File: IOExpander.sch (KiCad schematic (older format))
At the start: 2 parts

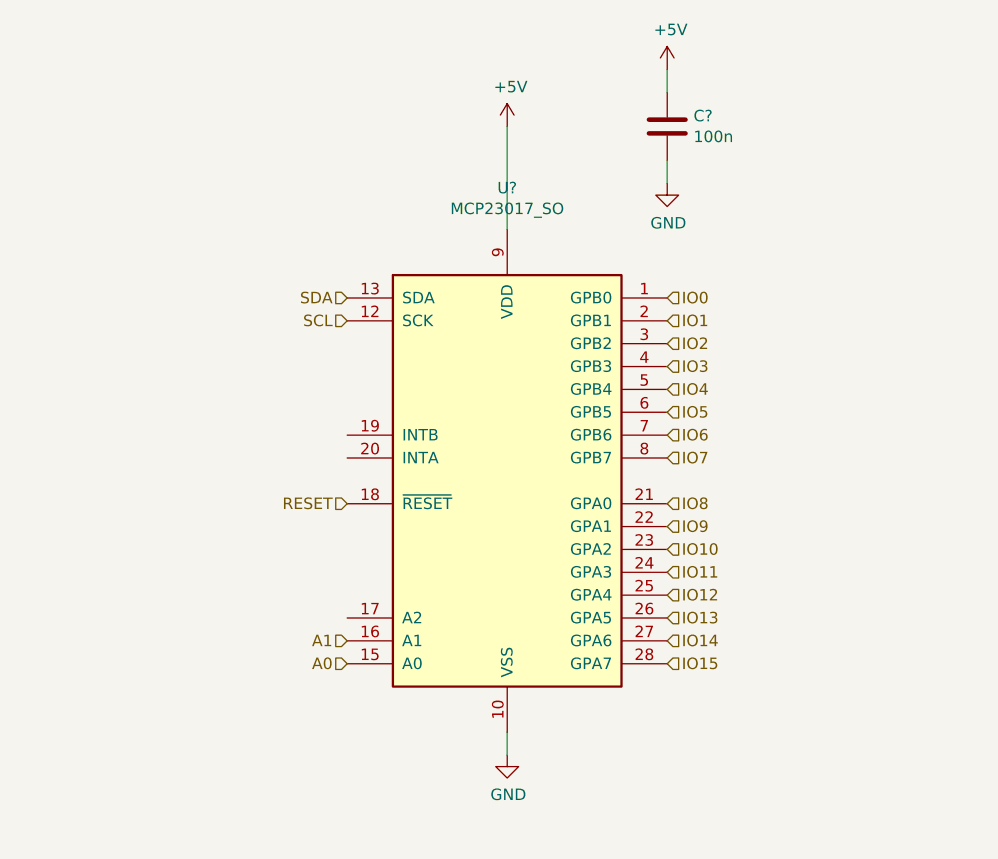
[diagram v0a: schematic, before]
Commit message: added display pinout
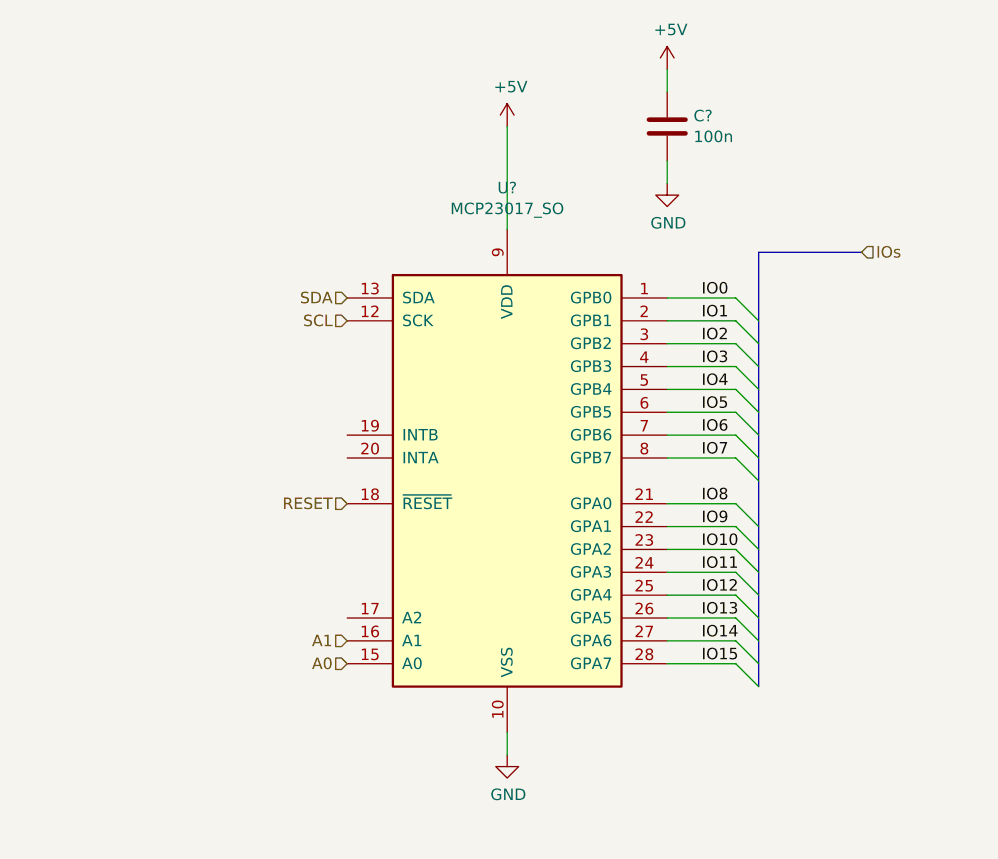
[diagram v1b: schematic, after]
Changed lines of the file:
@@
 $Descr A4 11693 8268
 encoding utf-8
-Sheet 4 4
+Sheet 4 6
 Title ""
 Date ""
@@
 Comment4 ""
 $EndDescr
-$Comp
-L Interface_Expansion:MCP23017_SO U?
-U 1 1 607270E1
-P 4450 3100
-F 0 "U?" H 4450 4381 50  0000 C CNN
-F 1 "MCP23017_SO" H 4450 4290 50  0000 C CNN
-F 2 "Package_SO:SOIC-28W_7.5x17.9mm_P1.27mm" H 4650 2100 50  0001 L CNN
-F 3 "http://ww1.microchip.com/downloads/en/DeviceDoc/20001952C.pdf" H 4650 2000 50  0001 L CNN
-	1    4450 3100
-	1    0    0    -1
-$EndComp
 Text HLabel 3750 2300 0    50   Input ~ 0
 SDA
@@
 U 1 1 607285C4
 P 4450 4300
+AR Path="/607267A8/607285C4" Ref="#PWR?"  Part="1"
+AR Path="/60679D69/607285C4" Ref="#PWR?"  Part="1"
 F 0 "#PWR?" H 4450 4050 50  0001 C CNN
 F 1 "GND" H 4455 4127 50  0000 C CNN
@@
 U 1 1 60728B72
 P 4450 1550
+AR Path="/607267A8/60728B72" Ref="#PWR?"  Part="1"
+AR Path="/60679D69/60728B72" Ref="#PWR?"  Part="1"
 F 0 "#PWR?" H 4450 1400 50  0001 C CNN
 F 1 "+5V" H 4465 1723 50  0000 C CNN
@@
 U 1 1 60729756
 P 5150 1550
+AR Path="/607267A8/60729756" Ref="C?"  Part="1"
+AR Path="/60679D69/60729756" Ref="C?"  Part="1"
 F 0 "C?" H 5265 1596 50  0000 L CNN
 F 1 "100n" H 5265 1505 50  0000 L CNN
@@
 U 1 1 60729F21
 P 5150 1300
+AR Path="/607267A8/60729F21" Ref="#PWR?"  Part="1"
+AR Path="/60679D69/60729F21" Ref="#PWR?"  Part="1"
 F 0 "#PWR?" H 5150 1150 50  0001 C CNN
 F 1 "+5V" H 5165 1473 50  0000 C CNN
@@
 U 1 1 6072A25B
 P 5150 1800
+AR Path="/607267A8/6072A25B" Ref="#PWR?"  Part="1"
+AR Path="/60679D69/6072A25B" Ref="#PWR?"  Part="1"
 F 0 "#PWR?" H 5150 1550 50  0001 C CNN
 F 1 "GND" H 5155 1627 50  0000 C CNN
@@
 Wire Wire Line
 	5150 1700 5150 1800
-Text HLabel 5150 2300 2    50   Input ~ 0
+$Comp
+L Interface_Expansion:MCP23017_SO U?
+U 1 1 607270E1
+P 4450 3100
+AR Path="/607267A8/607270E1" Ref="U?"  Part="1"
+AR Path="/60679D69/607270E1" Ref="U?"  Part="1"
+F 0 "U?" H 4450 4381 50  0000 C CNN
+F 1 "MCP23017_SO" H 4450 4290 50  0000 C CNN
+F 2 "Package_SO:SOIC-28W_7.5x17.9mm_P1.27mm" H 4650 2100 50  0001 L CNN
+F 3 "http://ww1.microchip.com/downloads/en/DeviceDoc/20001952C.pdf" H 4650 2000 50  0001 L CNN
+	1    4450 3100
+	1    0    0    -1
+$EndComp
+Wire Wire Line
+	5450 2300 5150 2300
+Wire Wire Line
+	5450 2400 5150 2400
+Wire Wire Line
+	5450 2500 5150 2500
+Wire Wire Line
+	5450 2600 5150 2600
+Wire Wire Line
+	5450 2700 5150 2700
+Wire Wire Line
+	5450 2800 5150 2800
+Wire Wire Line
+	5450 2900 5150 2900
+Wire Wire Line
+	5450 3000 5150 3000
+Wire Wire Line
+	5450 3200 5150 3200
+Wire Wire Line
+	5450 3300 5150 3300
+Wire Wire Line
+	5450 3400 5150 3400
+Wire Wire Line
+	5450 3500 5150 3500
+Wire Wire Line
+	5450 3600 5150 3600
+Wire Wire Line
+	5450 3700 5150 3700
+Wire Wire Line
+	5450 3800 5150 3800
+Wire Wire Line
+	5450 3900 5150 3900
+Wire Bus Line
+	5550 2100 6000 2100
+Entry Wire Line
+	5450 2300 5550 2400
+Entry Wire Line
+	5450 2400 5550 2500
+Entry Wire Line
+	5450 2500 5550 2600
+Entry Wire Line
+	5450 2600 5550 2700
+Entry Wire Line
+	5450 2700 5550 2800
+Entry Wire Line
+	5450 2800 5550 2900
+Entry Wire Line
+	5450 2900 5550 3000
+Entry Wire Line
+	5450 3000 5550 3100
+Entry Wire Line
+	5450 3200 5550 3300
+Entry Wire Line
+	5450 3300 5550 3400
+Entry Wire Line
+	5450 3400 5550 3500
+Entry Wire Line
+	5450 3500 5550 3600
+Entry Wire Line
+	5450 3600 5550 3700
+Entry Wire Line
+	5450 3700 5550 3800
+Entry Wire Line
+	5450 3800 5550 3900
+Entry Wire Line
+	5450 3900 5550 4000
+Wire Bus Line
+	5550 2100 5550 4000
+Text HLabel 6000 2100 2    50   Input ~ 0
+IOs
+Text Label 5300 2300 0    50   ~ 0
 IO0
-Text HLabel 5150 2400 2    50   Input ~ 0
+Text Label 5300 2400 0    50   ~ 0
 IO1
-Text HLabel 5150 2500 2    50   Input ~ 0
+Text Label 5300 2500 0    50   ~ 0
 IO2
-Text HLabel 5150 2600 2    50   Input ~ 0
+Text Label 5300 2600 0    50   ~ 0
 IO3
-Text HLabel 5150 2700 2    50   Input ~ 0
+Text Label 5300 2700 0    50   ~ 0
 IO4
-Text HLabel 5150 2800 2    50   Input ~ 0
+Text Label 5300 2800 0    50   ~ 0
 IO5
-Text HLabel 5150 2900 2    50   Input ~ 0
+Text Label 5300 2900 0    50   ~ 0
 IO6
-Text HLabel 5150 3000 2    50   Input ~ 0
+Text Label 5300 3000 0    50   ~ 0
 IO7
-Text HLabel 5150 3200 2    50   Input ~ 0
+Text Label 5300 3200 0    50   ~ 0
 IO8
-Text HLabel 5150 3300 2    50   Input ~ 0
+Text Label 5300 3300 0    50   ~ 0
 IO9
-Text HLabel 5150 3400 2    50   Input ~ 0
+Text Label 5300 3400 0    50   ~ 0
 IO10
-Text HLabel 5150 3500 2    50   Input ~ 0
+Text Label 5300 3500 0    50   ~ 0
 IO11
-Text HLabel 5150 3600 2    50   Input ~ 0
+Text Label 5300 3600 0    50   ~ 0
 IO12
-Text HLabel 5150 3700 2    50   Input ~ 0
+Text Label 5300 3700 0    50   ~ 0
 IO13
-Text HLabel 5150 3800 2    50   Input ~ 0
+Text Label 5300 3800 0    50   ~ 0
 IO14
-Text HLabel 5150 3900 2    50   Input ~ 0
+Text Label 5300 3900 0    50   ~ 0
 IO15
 $EndSCHEMATC

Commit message: added rj45 input
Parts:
- added R? (x4): R, symbol AR2ISS:R
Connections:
- net A0 is gone; now on net GND: U?.15 (A0)
- net +5V: now also R?.1, R?.1
- net GND: now also R?.2, R?.2
- net at U?.17 (A2): now also R?.1, R?.2
- net A1: no longer names the net of U?.16 (A1)
- net A1: now also R?.1, R?.2
- no-connect marks 0 -> 2
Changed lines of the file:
@@
 $Descr A4 11693 8268
 encoding utf-8
-Sheet 4 6
+Sheet 4 7
 Title ""
 Date ""
@@
 Comment4 ""
 $EndDescr
-Text HLabel 3750 2300 0    50   Input ~ 0
+Text HLabel 3650 2300 0    50   Input ~ 0
 SDA
-Text HLabel 3750 2400 0    50   Input ~ 0
+Text HLabel 3650 2400 0    50   Input ~ 0
 SCL
-Text HLabel 3750 3200 0    50   Input ~ 0
+Text HLabel 3650 3200 0    50   Input ~ 0
 RESET
-Text HLabel 3750 3900 0    50   Input ~ 0
-A0
-Text HLabel 3750 3800 0    50   Input ~ 0
-A1
 $Comp
 L power:GND #PWR?
@@
 Wire Wire Line
 	5150 1700 5150 1800
-$Comp
-L Interface_Expansion:MCP23017_SO U?
-U 1 1 607270E1
-P 4450 3100
-AR Path="/607267A8/607270E1" Ref="U?"  Part="1"
-AR Path="/60679D69/607270E1" Ref="U?"  Part="1"
-F 0 "U?" H 4450 4381 50  0000 C CNN
-F 1 "MCP23017_SO" H 4450 4290 50  0000 C CNN
-F 2 "Package_SO:SOIC-28W_7.5x17.9mm_P1.27mm" H 4650 2100 50  0001 L CNN
-F 3 "http://ww1.microchip.com/downloads/en/DeviceDoc/20001952C.pdf" H 4650 2000 50  0001 L CNN
-	1    4450 3100
-	1    0    0    -1
-$EndComp
 Wire Wire Line
 	5450 2300 5150 2300
@@
 Entry Wire Line
 	5450 3900 5550 4000
-Wire Bus Line
-	5550 2100 5550 4000
 Text HLabel 6000 2100 2    50   Input ~ 0
 IOs
@@
 Text Label 5300 3900 0    50   ~ 0
 IO15
+Text Label 5600 2100 0    50   ~ 0
+IO[0..15]
+$Comp
+L power:GND #PWR?
+U 1 1 607ACAD8
+P 2900 4450
+AR Path="/607267A8/607ACAD8" Ref="#PWR?"  Part="1"
+AR Path="/60679D69/607ACAD8" Ref="#PWR?"  Part="1"
+F 0 "#PWR?" H 2900 4200 50  0001 C CNN
+F 1 "GND" H 2905 4277 50  0000 C CNN
+F 2 "" H 2900 4450 50  0001 C CNN
+F 3 "" H 2900 4450 50  0001 C CNN
+	1    2900 4450
+	1    0    0    -1
+$EndComp
+$Comp
+L AR2ISS:R R?
+U 1 1 607B188F
+P 2650 4200
+AR Path="/60679D69/607B188F" Ref="R?"  Part="1"
+AR Path="/607267A8/607B188F" Ref="R?"  Part="1"
+F 0 "R?" H 2720 4246 50  0000 L CNN
+F 1 "R" H 2720 4155 50  0000 L CNN
+F 2 "" V 2580 4200 50  0001 C CNN
+F 3 "~" H 2650 4200 50  0001 C CNN
+	1    2650 4200
+	1    0    0    -1
+$EndComp
+$Comp
+L power:GND #PWR?
+U 1 1 607B1895
+P 2650 4450
+AR Path="/607267A8/607B1895" Ref="#PWR?"  Part="1"
+AR Path="/60679D69/607B1895" Ref="#PWR?"  Part="1"
+F 0 "#PWR?" H 2650 4200 50  0001 C CNN
+F 1 "GND" H 2655 4277 50  0000 C CNN
+F 2 "" H 2650 4450 50  0001 C CNN
+F 3 "" H 2650 4450 50  0001 C CNN
+	1    2650 4450
+	1    0    0    -1
+$EndComp
+Wire Wire Line
+	2650 4350 2650 4450
+$Comp
+L AR2ISS:R R?
+U 1 1 607B24D6
+P 2400 4200
+AR Path="/60679D69/607B24D6" Ref="R?"  Part="1"
+AR Path="/607267A8/607B24D6" Ref="R?"  Part="1"
+F 0 "R?" H 2470 4246 50  0000 L CNN
+F 1 "R" H 2470 4155 50  0000 L CNN
+F 2 "" V 2330 4200 50  0001 C CNN
+F 3 "~" H 2400 4200 50  0001 C CNN
+	1    2400 4200
+	1    0    0    -1
+$EndComp
+$Comp
+L power:GND #PWR?
+U 1 1 607B24DC
+P 2400 4450
+AR Path="/607267A8/607B24DC" Ref="#PWR?"  Part="1"
+AR Path="/60679D69/607B24DC" Ref="#PWR?"  Part="1"
+F 0 "#PWR?" H 2400 4200 50  0001 C CNN
+F 1 "GND" H 2405 4277 50  0000 C CNN
+F 2 "" H 2400 4450 50  0001 C CNN
+F 3 "" H 2400 4450 50  0001 C CNN
+	1    2400 4450
+	1    0    0    -1
+$EndComp
+Wire Wire Line
+	2400 4350 2400 4450
+$Comp
+L AR2ISS:R R?
+U 1 1 607B4040
+P 2650 3450
+AR Path="/60679D69/607B4040" Ref="R?"  Part="1"
+AR Path="/607267A8/607B4040" Ref="R?"  Part="1"
+F 0 "R?" H 2720 3496 50  0000 L CNN
+F 1 "R" H 2720 3405 50  0000 L CNN
+F 2 "" V 2580 3450 50  0001 C CNN
+F 3 "~" H 2650 3450 50  0001 C CNN
+	1    2650 3450
+	1    0    0    -1
+$EndComp
+$Comp
+L power:+5V #PWR?
+U 1 1 607B4046
+P 2650 3200
+AR Path="/607267A8/607B4046" Ref="#PWR?"  Part="1"
+AR Path="/60679D69/607B4046" Ref="#PWR?"  Part="1"
+F 0 "#PWR?" H 2650 3050 50  0001 C CNN
+F 1 "+5V" H 2665 3373 50  0000 C CNN
+F 2 "" H 2650 3200 50  0001 C CNN
+F 3 "" H 2650 3200 50  0001 C CNN
+	1    2650 3200
+	1    0    0    -1
+$EndComp
+Wire Wire Line
+	2650 3200 2650 3300
+$Comp
+L AR2ISS:R R?
+U 1 1 607B4D77
+P 2400 3450
+AR Path="/60679D69/607B4D77" Ref="R?"  Part="1"
+AR Path="/607267A8/607B4D77" Ref="R?"  Part="1"
+F 0 "R?" H 2470 3496 50  0000 L CNN
+F 1 "R" H 2470 3405 50  0000 L CNN
+F 2 "" V 2330 3450 50  0001 C CNN
+F 3 "~" H 2400 3450 50  0001 C CNN
+	1    2400 3450
+	1    0    0    -1
+$EndComp
+$Comp
+L power:+5V #PWR?
+U 1 1 607B4D7D
+P 2400 3200
+AR Path="/607267A8/607B4D7D" Ref="#PWR?"  Part="1"
+AR Path="/60679D69/607B4D7D" Ref="#PWR?"  Part="1"
+F 0 "#PWR?" H 2400 3050 50  0001 C CNN
+F 1 "+5V" H 2415 3373 50  0000 C CNN
+F 2 "" H 2400 3200 50  0001 C CNN
+F 3 "" H 2400 3200 50  0001 C CNN
+	1    2400 3200
+	1    0    0    -1
+$EndComp
+Wire Wire Line
+	2400 3200 2400 3300
+Wire Wire Line
+	2400 3700 2400 3600
+Wire Wire Line
+	2400 3700 2400 4050
+Connection ~ 2400 3700
+Wire Wire Line
+	2650 3800 2650 3600
+Wire Wire Line
+	2650 4050 2650 3800
+Connection ~ 2650 3800
+NoConn ~ 3750 3000
+Wire Wire Line
+	2900 3900 2900 4450
+Wire Wire Line
+	2400 3700 3750 3700
+Wire Wire Line
+	2650 3800 3750 3800
+Wire Wire Line
+	2900 3900 3750 3900
+Wire Wire Line
+	3650 2300 3750 2300
+Wire Wire Line
+	3650 3200 3750 3200
+Wire Wire Line
+	3650 2400 3750 2400
+$Comp
+L Interface_Expansion:MCP23017_SO U?
+U 1 1 607270E1
+P 4450 3100
+AR Path="/607267A8/607270E1" Ref="U?"  Part="1"
+AR Path="/60679D69/607270E1" Ref="U?"  Part="1"
+F 0 "U?" H 4450 4381 50  0000 C CNN
+F 1 "MCP23017_SO" H 4450 4290 50  0000 C CNN
+F 2 "Package_SO:SOIC-28W_7.5x17.9mm_P1.27mm" H 4650 2100 50  0001 L CNN
+F 3 "http://ww1.microchip.com/downloads/en/DeviceDoc/20001952C.pdf" H 4650 2000 50  0001 L CNN
+	1    4450 3100
+	1    0    0    -1
+$EndComp
+NoConn ~ 3750 2900
+Wire Bus Line
+	5550 2100 5550 4000
 $EndSCHEMATC

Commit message: first layout
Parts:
- C18: renamed from C?; footprint (none) -> Capacitor_SMD:C_0603_1608Metric
- R12, R13, R14, R15: renamed from R?; footprint (none) -> Resistor_SMD:R_0603_1608Metric
- gave numbers to parts that had none: 1
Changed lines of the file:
@@
 $Descr A4 11693 8268
 encoding utf-8
-Sheet 6 9
+Sheet 5 17
 Title ""
 Date ""
@@
 RESET
 $Comp
-L power:GND #PWR?
+L power:GND #PWR060
 U 1 1 607285C4
 P 4450 4300
-AR Path="/607267A8/607285C4" Ref="#PWR?"  Part="1"
-AR Path="/60679D69/607285C4" Ref="#PWR?"  Part="1"
-F 0 "#PWR?" H 4450 4050 50  0001 C CNN
+AR Path="/607267A8/607285C4" Ref="#PWR060"  Part="1"
+AR Path="/60679D69/607285C4" Ref="#PWR032"  Part="1"
+F 0 "#PWR060" H 4450 4050 50  0001 C CNN
 F 1 "GND" H 4455 4127 50  0000 C CNN
 F 2 "" H 4450 4300 50  0001 C CNN
@@
 $EndComp
 $Comp
-L power:+5V #PWR?
+L power:+5V #PWR059
 U 1 1 60728B72
 P 4450 1550
-AR Path="/607267A8/60728B72" Ref="#PWR?"  Part="1"
-AR Path="/60679D69/60728B72" Ref="#PWR?"  Part="1"
-F 0 "#PWR?" H 4450 1400 50  0001 C CNN
+AR Path="/607267A8/60728B72" Ref="#PWR059"  Part="1"
+AR Path="/60679D69/60728B72" Ref="#PWR031"  Part="1"
+F 0 "#PWR059" H 4450 1400 50  0001 C CNN
 F 1 "+5V" H 4465 1723 50  0000 C CNN
 F 2 "" H 4450 1550 50  0001 C CNN
@@
 	4450 4200 4450 4300
 $Comp
-L AR2ISS:C C?
+L AR2ISS:C C18
 U 1 1 60729756
 P 5150 1550
-AR Path="/607267A8/60729756" Ref="C?"  Part="1"
-AR Path="/60679D69/60729756" Ref="C?"  Part="1"
-F 0 "C?" H 5265 1596 50  0000 L CNN
+AR Path="/607267A8/60729756" Ref="C18"  Part="1"
+AR Path="/60679D69/60729756" Ref="C14"  Part="1"
+F 0 "C18" H 5265 1596 50  0000 L CNN
 F 1 "100n" H 5265 1505 50  0000 L CNN
-F 2 "" H 5188 1400 50  0001 C CNN
+F 2 "Capacitor_SMD:C_0603_1608Metric" H 5188 1400 50  0001 C CNN
 F 3 "~" H 5150 1550 50  0001 C CNN
 	1    5150 1550
@@
 $EndComp
 $Comp
-L power:+5V #PWR?
+L power:+5V #PWR061
 U 1 1 60729F21
 P 5150 1300
-AR Path="/607267A8/60729F21" Ref="#PWR?"  Part="1"
-AR Path="/60679D69/60729F21" Ref="#PWR?"  Part="1"
-F 0 "#PWR?" H 5150 1150 50  0001 C CNN
+AR Path="/607267A8/60729F21" Ref="#PWR061"  Part="1"
+AR Path="/60679D69/60729F21" Ref="#PWR033"  Part="1"
+F 0 "#PWR061" H 5150 1150 50  0001 C CNN
 F 1 "+5V" H 5165 1473 50  0000 C CNN
 F 2 "" H 5150 1300 50  0001 C CNN
@@
 $EndComp
 $Comp
-L power:GND #PWR?
+L power:GND #PWR062
 U 1 1 6072A25B
 P 5150 1800
-AR Path="/607267A8/6072A25B" Ref="#PWR?"  Part="1"
-AR Path="/60679D69/6072A25B" Ref="#PWR?"  Part="1"
-F 0 "#PWR?" H 5150 1550 50  0001 C CNN
+AR Path="/607267A8/6072A25B" Ref="#PWR062"  Part="1"
+AR Path="/60679D69/6072A25B" Ref="#PWR034"  Part="1"
+F 0 "#PWR062" H 5150 1550 50  0001 C CNN
 F 1 "GND" H 5155 1627 50  0000 C CNN
 F 2 "" H 5150 1800 50  0001 C CNN
@@
 Entry Wire Line
 	5450 3900 5550 4000
-Text HLabel 6000 2100 2    50   Input ~ 0
-IOs
+Text HLabel 6000 2100 2    50   Output ~ 0
+IO[0..15]
 Text Label 5300 2300 0    50   ~ 0
 IO0
@@
 IO[0..15]
 $Comp
-L power:GND #PWR?
+L power:GND #PWR058
 U 1 1 607ACAD8
 P 2900 4450
-AR Path="/607267A8/607ACAD8" Ref="#PWR?"  Part="1"
-AR Path="/60679D69/607ACAD8" Ref="#PWR?"  Part="1"
-F 0 "#PWR?" H 2900 4200 50  0001 C CNN
+AR Path="/607267A8/607ACAD8" Ref="#PWR058"  Part="1"
+AR Path="/60679D69/607ACAD8" Ref="#PWR030"  Part="1"
+F 0 "#PWR058" H 2900 4200 50  0001 C CNN
 F 1 "GND" H 2905 4277 50  0000 C CNN
 F 2 "" H 2900 4450 50  0001 C CNN
@@
 $EndComp
 $Comp
-L AR2ISS:R R?
+L AR2ISS:R R15
 U 1 1 607B188F
 P 2650 4200
-AR Path="/60679D69/607B188F" Ref="R?"  Part="1"
-AR Path="/607267A8/607B188F" Ref="R?"  Part="1"
-F 0 "R?" H 2720 4246 50  0000 L CNN
+AR Path="/60679D69/607B188F" Ref="R15"  Part="1"
+AR Path="/607267A8/607B188F" Ref="R40"  Part="1"
+F 0 "R40" H 2720 4246 50  0000 L CNN
 F 1 "R" H 2720 4155 50  0000 L CNN
-F 2 "" V 2580 4200 50  0001 C CNN
+F 2 "Resistor_SMD:R_0603_1608Metric" V 2580 4200 50  0001 C CNN
 F 3 "~" H 2650 4200 50  0001 C CNN
 	1    2650 4200
@@
 $EndComp
 $Comp
-L power:GND #PWR?
+L power:GND #PWR057
 U 1 1 607B1895
 P 2650 4450
-AR Path="/607267A8/607B1895" Ref="#PWR?"  Part="1"
-AR Path="/60679D69/607B1895" Ref="#PWR?"  Part="1"
-F 0 "#PWR?" H 2650 4200 50  0001 C CNN
+AR Path="/607267A8/607B1895" Ref="#PWR057"  Part="1"
+AR Path="/60679D69/607B1895" Ref="#PWR029"  Part="1"
+F 0 "#PWR057" H 2650 4200 50  0001 C CNN
 F 1 "GND" H 2655 4277 50  0000 C CNN
 F 2 "" H 2650 4450 50  0001 C CNN
@@
 	2650 4350 2650 4450
 $Comp
-L AR2ISS:R R?
+L AR2ISS:R R13
 U 1 1 607B24D6
 P 2400 4200
-AR Path="/60679D69/607B24D6" Ref="R?"  Part="1"
-AR Path="/607267A8/607B24D6" Ref="R?"  Part="1"
-F 0 "R?" H 2470 4246 50  0000 L CNN
+AR Path="/60679D69/607B24D6" Ref="R13"  Part="1"
+AR Path="/607267A8/607B24D6" Ref="R38"  Part="1"
+F 0 "R38" H 2470 4246 50  0000 L CNN
 F 1 "R" H 2470 4155 50  0000 L CNN
-F 2 "" V 2330 4200 50  0001 C CNN
+F 2 "Resistor_SMD:R_0603_1608Metric" V 2330 4200 50  0001 C CNN
 F 3 "~" H 2400 4200 50  0001 C CNN
 	1    2400 4200
@@
 $EndComp
 $Comp
-L power:GND #PWR?
+L power:GND #PWR055
 U 1 1 607B24DC
 P 2400 4450
-AR Path="/607267A8/607B24DC" Ref="#PWR?"  Part="1"
-AR Path="/60679D69/607B24DC" Ref="#PWR?"  Part="1"
-F 0 "#PWR?" H 2400 4200 50  0001 C CNN
+AR Path="/607267A8/607B24DC" Ref="#PWR055"  Part="1"
+AR Path="/60679D69/607B24DC" Ref="#PWR027"  Part="1"
+F 0 "#PWR055" H 2400 4200 50  0001 C CNN
 F 1 "GND" H 2405 4277 50  0000 C CNN
 F 2 "" H 2400 4450 50  0001 C CNN
@@
 	2400 4350 2400 4450
 $Comp
-L AR2ISS:R R?
+L AR2ISS:R R14
 U 1 1 607B4040
 P 2650 3450
-AR Path="/60679D69/607B4040" Ref="R?"  Part="1"
-AR Path="/607267A8/607B4040" Ref="R?"  Part="1"
-F 0 "R?" H 2720 3496 50  0000 L CNN
+AR Path="/60679D69/607B4040" Ref="R14"  Part="1"
+AR Path="/607267A8/607B4040" Ref="R39"  Part="1"
+F 0 "R39" H 2720 3496 50  0000 L CNN
 F 1 "R" H 2720 3405 50  0000 L CNN
-F 2 "" V 2580 3450 50  0001 C CNN
+F 2 "Resistor_SMD:R_0603_1608Metric" V 2580 3450 50  0001 C CNN
 F 3 "~" H 2650 3450 50  0001 C CNN
 	1    2650 3450
@@
 $EndComp
 $Comp
-L power:+5V #PWR?
+L power:+5V #PWR056
 U 1 1 607B4046
 P 2650 3200
-AR Path="/607267A8/607B4046" Ref="#PWR?"  Part="1"
-AR Path="/60679D69/607B4046" Ref="#PWR?"  Part="1"
-F 0 "#PWR?" H 2650 3050 50  0001 C CNN
+AR Path="/607267A8/607B4046" Ref="#PWR056"  Part="1"
+AR Path="/60679D69/607B4046" Ref="#PWR028"  Part="1"
+F 0 "#PWR056" H 2650 3050 50  0001 C CNN
 F 1 "+5V" H 2665 3373 50  0000 C CNN
 F 2 "" H 2650 3200 50  0001 C CNN
@@
 	2650 3200 2650 3300
 $Comp
-L AR2ISS:R R?
+L AR2ISS:R R12
 U 1 1 607B4D77
 P 2400 3450
-AR Path="/60679D69/607B4D77" Ref="R?"  Part="1"
-AR Path="/607267A8/607B4D77" Ref="R?"  Part="1"
-F 0 "R?" H 2470 3496 50  0000 L CNN
+AR Path="/60679D69/607B4D77" Ref="R12"  Part="1"
+AR Path="/607267A8/607B4D77" Ref="R37"  Part="1"
+F 0 "R37" H 2470 3496 50  0000 L CNN
 F 1 "R" H 2470 3405 50  0000 L CNN
-F 2 "" V 2330 3450 50  0001 C CNN
+F 2 "Resistor_SMD:R_0603_1608Metric" V 2330 3450 50  0001 C CNN
 F 3 "~" H 2400 3450 50  0001 C CNN
 	1    2400 3450
@@
 $EndComp
 $Comp
-L power:+5V #PWR?
+L power:+5V #PWR054
 U 1 1 607B4D7D
 P 2400 3200
-AR Path="/607267A8/607B4D7D" Ref="#PWR?"  Part="1"
-AR Path="/60679D69/607B4D7D" Ref="#PWR?"  Part="1"
-F 0 "#PWR?" H 2400 3050 50  0001 C CNN
+AR Path="/607267A8/607B4D7D" Ref="#PWR054"  Part="1"
+AR Path="/60679D69/607B4D7D" Ref="#PWR026"  Part="1"
+F 0 "#PWR054" H 2400 3050 50  0001 C CNN
 F 1 "+5V" H 2415 3373 50  0000 C CNN
 F 2 "" H 2400 3200 50  0001 C CNN
@@
 	3650 2400 3750 2400
 $Comp
-L Interface_Expansion:MCP23017_SO U?
+L Interface_Expansion:MCP23017_SO U11
 U 1 1 607270E1
 P 4450 3100
-AR Path="/607267A8/607270E1" Ref="U?"  Part="1"
-AR Path="/60679D69/607270E1" Ref="U?"  Part="1"
-F 0 "U?" H 4450 4381 50  0000 C CNN
+AR Path="/607267A8/607270E1" Ref="U11"  Part="1"
+AR Path="/60679D69/607270E1" Ref="U8"  Part="1"
+F 0 "U11" H 4450 4381 50  0000 C CNN
 F 1 "MCP23017_SO" H 4450 4290 50  0000 C CNN
 F 2 "Package_SO:SOIC-28W_7.5x17.9mm_P1.27mm" H 4650 2100 50  0001 L CNN
